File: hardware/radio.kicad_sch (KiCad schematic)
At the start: 0 parts

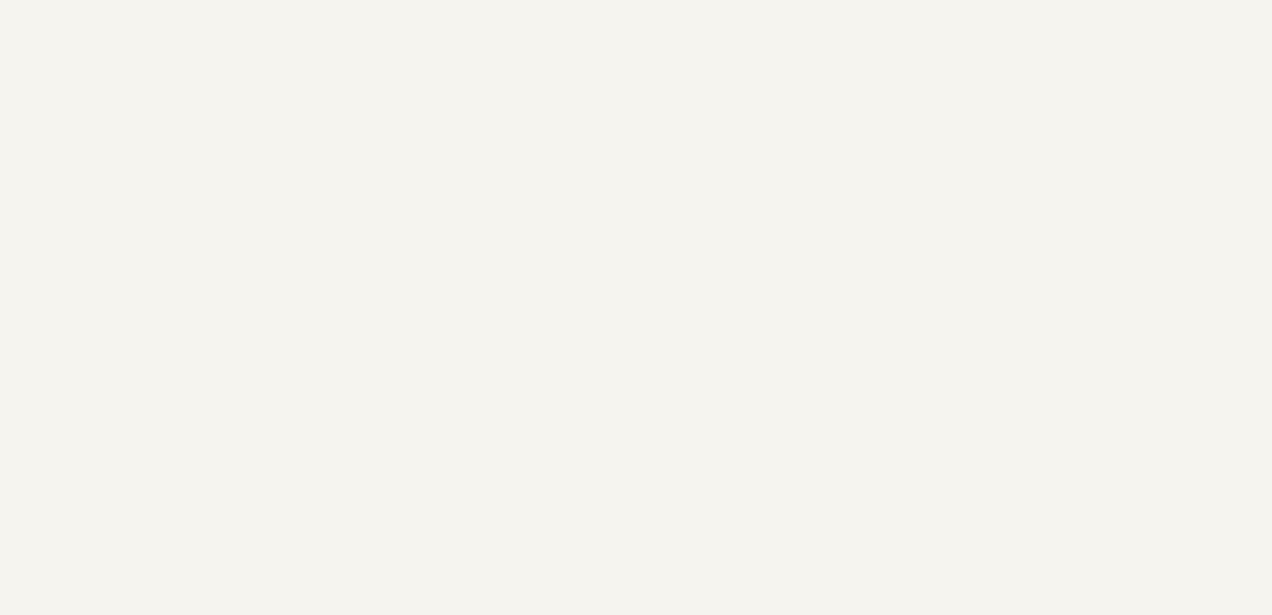
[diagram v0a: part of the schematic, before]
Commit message: stworzony symbol MAX98357
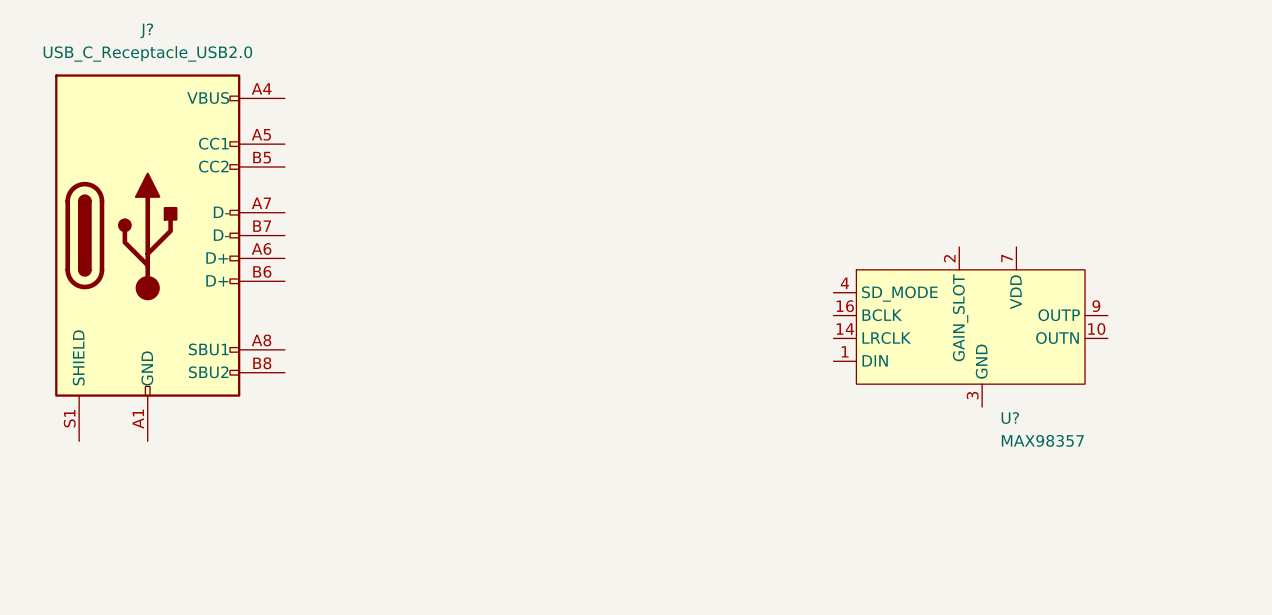
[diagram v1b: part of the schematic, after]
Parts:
- added J?: USB_C_Receptacle_USB2.0, symbol Connector:USB_C_Receptacle_USB2.0
- added U?: MAX98357, Package_DFN_QFN:TQFN-16-1EP_3x3mm_P0.5mm_EP1.23x1.23mm, symbol scalaki:MAX98357
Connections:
- new net: J?.A1 (GND), J?.A12 (GND), J?.B1 (GND), J?.B12 (GND)
- new net: J?.A4 (VBUS), J?.A9 (VBUS), J?.B4 (VBUS), J?.B9 (VBUS)
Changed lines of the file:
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@@
     (effects (font (size 1.27 1.27)) (justify left bottom))
+  )
+  (symbol (lib_id "scalaki:MAX98357") (at 138.43 53.34 0) (unit 1)
+    (in_bom yes) (on_board yes) (fields_autoplaced)
+    (property "Reference" "U?" (id 0) (at 140.4494 63.5 0)
+      (effects (font (size 1.27 1.27)) (justify left))
+    )
+    (property "Value" "MAX98357" (id 1) (at 140.4494 66.04 0)
+      (effects (font (size 1.27 1.27)) (justify left))
+    )
+    (property "Footprint" "Package_DFN_QFN:TQFN-16-1EP_3x3mm_P0.5mm_EP1.23x1.23mm" (id 2) (at 138.43 53.34 0)
+      (effects (font (size 1.27 1.27)) hide)
+    )
+    (property "Datasheet" "" (id 3) (at 138.43 53.34 0)
+      (effects (font (size 1.27 1.27)) hide)
+    )
+    (pin "1")
+    (pin "10")
+    (pin "14")
+    (pin "16")
+    (pin "2")
+    (pin "3")
+    (pin "4")
+    (pin "7")
+    (pin "9")
+  )
+  (symbol (lib_id "Connector:USB_C_Receptacle_USB2.0") (at 45.72 43.18 0) (unit 1)
+    (in_bom yes) (on_board yes) (fields_autoplaced)
+    (property "Reference" "J?" (id 0) (at 45.72 20.32 0))
+    (property "Value" "USB_C_Receptacle_USB2.0" (id 1) (at 45.72 22.86 0))
+    (property "Footprint" "" (id 2) (at 49.53 43.18 0)
+      (effects (font (size 1.27 1.27)) hide)
+    )
+    (property "Datasheet" "https://www.usb.org/sites/default/files/documents/usb_type-c.zip" (id 3) (at 49.53 43.18 0)
+      (effects (font (size 1.27 1.27)) hide)
+    )
+    (pin "A1")
+    (pin "A12")
+    (pin "A4")
+    (pin "A5")
+    (pin "A6")
+    (pin "A7")
+    (pin "A8")
+    (pin "A9")
+    (pin "B1")
+    (pin "B12")
+    (pin "B4")
+    (pin "B5")
+    (pin "B6")
+    (pin "B7")
+    (pin "B8")
+    (pin "B9")
+    (pin "S1")
   )
   (sheet_instances
     (path "/" (page "1"))
   )
+  (symbol_instances
+    (path "/8b0ef56b-3e26-4f83-b202-0d062c709ccb"
+      (reference "J?") (unit 1) (value "USB_C_Receptacle_USB2.0") (footprint "")
+    )
+    (path "/41e115bb-878b-4e97-96e4-aac5a3321929"
+      (reference "U?") (unit 1) (value "MAX98357") (footprint "Package_DFN_QFN:TQFN-16-1EP_3x3mm_P0.5mm_EP1.23x1.23mm")
+    )
+  )
 )

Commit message: utworzono symbol TPS5432
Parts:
- added U?: TP4056, symbol scalaki:TP4056
- added U?: TPS5432, Package_SO:TI_SO-PowerPAD-8, symbol scalaki:TPS5432
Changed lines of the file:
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@@
     (pin "S1")
+  )
+  (symbol (lib_id "scalaki:TP4056") (at 102.87 38.1 0) (unit 1)
+    (in_bom yes) (on_board yes) (fields_autoplaced)
+    (property "Reference" "U?" (id 0) (at 106.68 26.67 0))
+    (property "Value" "TP4056" (id 1) (at 106.68 29.21 0))
+    (property "Footprint" "" (id 2) (at 100.33 39.37 0)
+      (effects (font (size 1.27 1.27)) hide)
+    )
+    (property "Datasheet" "" (id 3) (at 100.33 39.37 0)
+      (effects (font (size 1.27 1.27)) hide)
+    )
+    (pin "1")
+    (pin "2")
+    (pin "3")
+    (pin "4")
+    (pin "5")
+    (pin "6")
+    (pin "7")
+    (pin "8")
+  )
+  (symbol (lib_id "scalaki:TPS5432") (at 185.42 52.07 0) (unit 1)
+    (in_bom yes) (on_board yes) (fields_autoplaced)
+    (property "Reference" "U?" (id 0) (at 187.325 36.83 0))
+    (property "Value" "TPS5432" (id 1) (at 187.325 39.37 0))
+    (property "Footprint" "Package_SO:TI_SO-PowerPAD-8" (id 2) (at 193.04 64.77 0)
+      (effects (font (size 1.27 1.27)) hide)
+    )
+    (property "Datasheet" "https://www.ti.com/lit/ds/slvsb89a/slvsb89a.pdf?ts=1654873515144&ref_url=https%253A%252F%252Fwww.google.com%252F" (id 3) (at 238.76 67.31 0)
+      (effects (font (size 1.27 1.27)) hide)
+    )
+    (pin "1")
+    (pin "2")
+    (pin "3")
+    (pin "4")
+    (pin "5")
+    (pin "6")
+    (pin "7")
+    (pin "8")
   )
   (sheet_instances
@@
       (reference "U?") (unit 1) (value "MAX98357") (footprint "Package_DFN_QFN:TQFN-16-1EP_3x3mm_P0.5mm_EP1.23x1.23mm")
     )
+    (path "/a274958a-ae53-4989-b48b-9f41b3964f32"
+      (reference "U?") (unit 1) (value "TP4056") (footprint "")
+    )
+    (path "/f1c0ab59-7fad-4029-b3df-f395b5dae87a"
+      (reference "U?") (unit 1) (value "TPS5432") (footprint "Package_SO:TI_SO-PowerPAD-8")
+    )
   )

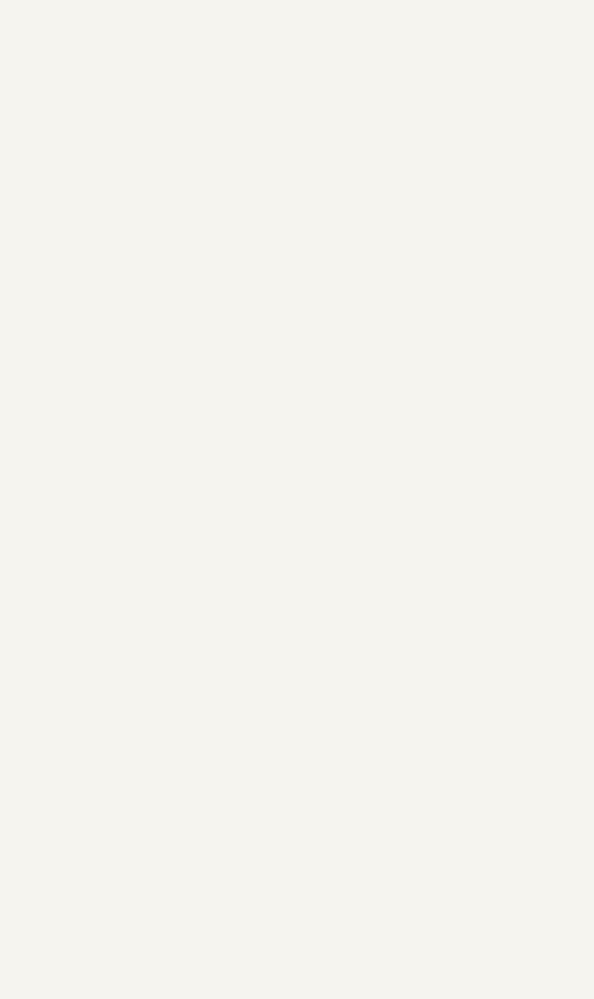
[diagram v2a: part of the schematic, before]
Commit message: dodano ESP32-WROOM-32 na schemacie
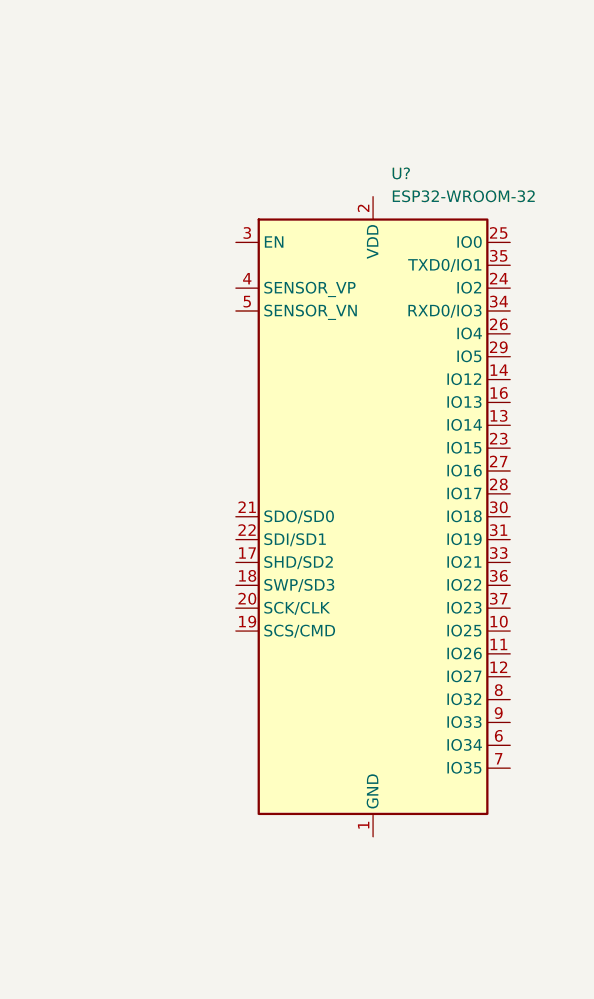
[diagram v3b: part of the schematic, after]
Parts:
- added U?: ESP32-WROOM-32, RF_Module:ESP32-WROOM-32, symbol RF_Module:ESP32-WROOM-32
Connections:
- new net: U?.1 (GND), U?.15 (GND), U?.38 (GND), U?.39 (GND)
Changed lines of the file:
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@@
+    (pin "9")
+  )
+  (symbol (lib_id "RF_Module:ESP32-WROOM-32") (at 240.03 85.09 0) (unit 1)
+    (in_bom yes) (on_board yes) (fields_autoplaced)
+    (property "Reference" "U?" (id 0) (at 242.0494 46.99 0)
+      (effects (font (size 1.27 1.27)) (justify left))
+    )
+    (property "Value" "ESP32-WROOM-32" (id 1) (at 242.0494 49.53 0)
+      (effects (font (size 1.27 1.27)) (justify left))
+    )
+    (property "Footprint" "RF_Module:ESP32-WROOM-32" (id 2) (at 240.03 123.19 0)
+      (effects (font (size 1.27 1.27)) hide)
+    )
+    (property "Datasheet" "https://www.espressif.com/sites/default/files/documentation/esp32-wroom-32_datasheet_en.pdf" (id 3) (at 232.41 83.82 0)
+      (effects (font (size 1.27 1.27)) hide)
+    )
+    (pin "1")
+    (pin "10")
+    (pin "11")
+    (pin "12")
+    (pin "13")
+    (pin "14")
+    (pin "15")
+    (pin "16")
+    (pin "17")
+    (pin "18")
+    (pin "19")
+    (pin "2")
+    (pin "20")
+    (pin "21")
+    (pin "22")
+    (pin "23")
+    (pin "24")
+    (pin "25")
+    (pin "26")
+    (pin "27")
+    (pin "28")
+    (pin "29")
+    (pin "3")
+    (pin "30")
+    (pin "31")
+    (pin "32")
+    (pin "33")
+    (pin "34")
+    (pin "35")
+    (pin "36")
+    (pin "37")
+    (pin "38")
+    (pin "39")
+    (pin "4")
+    (pin "5")
+    (pin "6")
+    (pin "7")
+    (pin "8")
     (pin "9")
   )
@@
       (reference "U?") (unit 1) (value "MAX98357") (footprint "Package_DFN_QFN:TQFN-16-1EP_3x3mm_P0.5mm_EP1.23x1.23mm")
     )
+    (path "/76beaedb-70bf-49f8-8321-692390a14d3f"
+      (reference "U?") (unit 1) (value "ESP32-WROOM-32") (footprint "RF_Module:ESP32-WROOM-32")
+    )
     (path "/a274958a-ae53-4989-b48b-9f41b3964f32"
